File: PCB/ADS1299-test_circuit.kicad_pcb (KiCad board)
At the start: 2 copper layers, 90.4 x 96.4 mm, 111 parts, among them J1 CONN_01X07, J2 CONN_01X01_MALE, J3 CONN_01X01_MALE, P1 +5V, P10 CONN_01X03, P11 CONN_01X03, P12 CONN_01X03, P13 CONN_01X03, P14 BiasOut_C, P15 BiasOut_R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

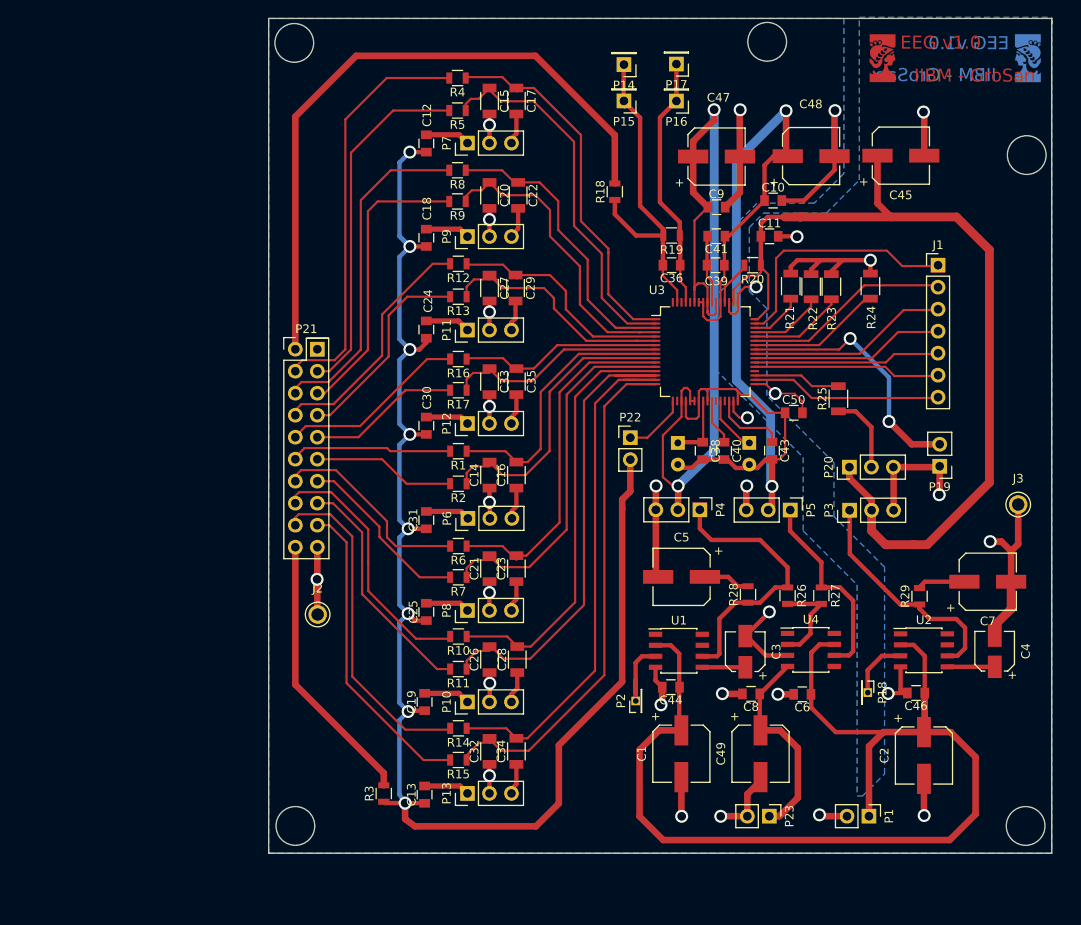
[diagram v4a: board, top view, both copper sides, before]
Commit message: Update Arduino and matlab code
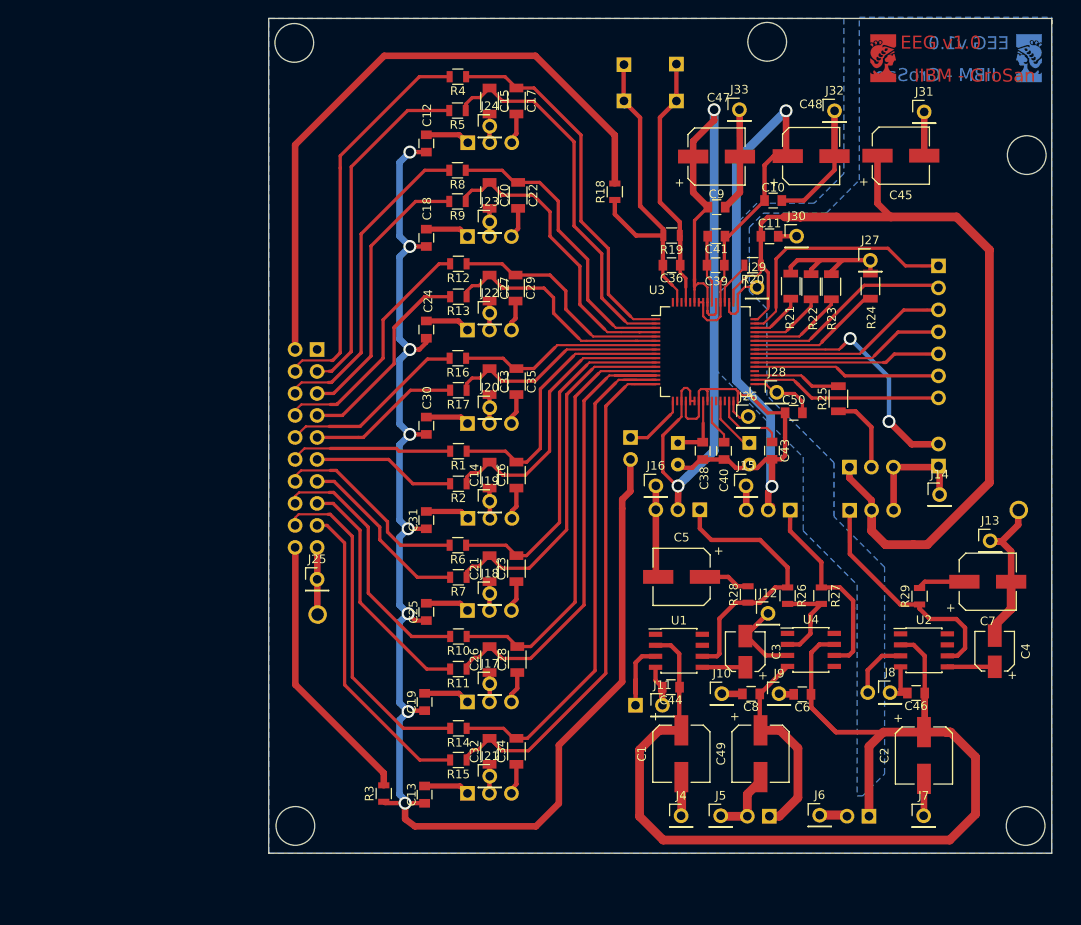
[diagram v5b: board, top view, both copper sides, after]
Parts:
- removed the G*** at (186.2, 29.0)
- removed the G*** at (202.9, 29.0)
- added G***: LOGO, LogoModules:logoFiuba_small_mirrored, F.Cu at (186.3, 29.0)
- added G***: LOGO, LogoModules:logoFiuba_small_mirrored, B.Cu at (203.1, 29.0)
- added J10: Via, Pin_Headers:Pin_Header_Straight_1x01_Pitch2.54mm, F.Cu at (167.6, 102.4)
- added J11: Via, Pin_Headers:Pin_Header_Straight_1x01_Pitch2.54mm, F.Cu at (160.8, 103.7)
- added J12: Via, Pin_Headers:Pin_Header_Straight_1x01_Pitch2.54mm, F.Cu at (173.0, 93.1)
- added J13: Via, Pin_Headers:Pin_Header_Straight_1x01_Pitch2.54mm, F.Cu at (198.6, 84.7)
- added J14: Via, Pin_Headers:Pin_Header_Straight_1x01_Pitch2.54mm, F.Cu at (192.8, 79.4)
- added J15: Via, Pin_Headers:Pin_Header_Straight_1x01_Pitch2.54mm, F.Cu at (170.4, 78.4)
- added J16: Via, Pin_Headers:Pin_Header_Straight_1x01_Pitch2.54mm, F.Cu at (160.0, 78.4)
- added J17: Via, Pin_Headers:Pin_Header_Straight_1x01_Pitch2.54mm, F.Cu at (140.8, 101.2)
- added J18: Via, Pin_Headers:Pin_Header_Straight_1x01_Pitch2.54mm, F.Cu at (140.8, 90.8)
- added J19: Via, Pin_Headers:Pin_Header_Straight_1x01_Pitch2.54mm, F.Cu at (140.8, 80.1)
- added J20: Via, Pin_Headers:Pin_Header_Straight_1x01_Pitch2.54mm, F.Cu at (140.8, 69.3)
- added J21: Via, Pin_Headers:Pin_Header_Straight_1x01_Pitch2.54mm, F.Cu at (140.8, 111.9)
- added J22: Via, Pin_Headers:Pin_Header_Straight_1x01_Pitch2.54mm, F.Cu at (140.8, 58.4)
- added J23: Via, Pin_Headers:Pin_Header_Straight_1x01_Pitch2.54mm, F.Cu at (140.8, 47.9)
- added J24: Via, Pin_Headers:Pin_Header_Straight_1x01_Pitch2.54mm, F.Cu at (140.8, 36.8)
- added J25: Via, Pin_Headers:Pin_Header_Straight_1x01_Pitch2.54mm, F.Cu at (120.9, 89.2)
- added J26: Via, Pin_Headers:Pin_Header_Straight_1x01_Pitch2.54mm, F.Cu at (170.7, 70.4)
- added J27: Via, Pin_Headers:Pin_Header_Straight_1x01_Pitch2.54mm, F.Cu at (184.8, 52.3)
- added J28: Via, Pin_Headers:Pin_Header_Straight_1x01_Pitch2.54mm, F.Cu at (174.0, 67.6)
- added J29: Via, Pin_Headers:Pin_Header_Straight_1x01_Pitch2.54mm, F.Cu at (171.7, 55.4)
- added J30: Via, Pin_Headers:Pin_Header_Straight_1x01_Pitch2.54mm, F.Cu at (176.3, 49.5)
- added J31: Via, Pin_Headers:Pin_Header_Straight_1x01_Pitch2.54mm, F.Cu at (191.0, 35.2)
- added J32: Via, Pin_Headers:Pin_Header_Straight_1x01_Pitch2.54mm, F.Cu at (180.7, 35.1)
- added J33: Via, Pin_Headers:Pin_Header_Straight_1x01_Pitch2.54mm, F.Cu at (169.7, 34.9)
- added J4: Via, Pin_Headers:Pin_Header_Straight_1x01_Pitch2.54mm, F.Cu at (162.9, 116.5)
- added J5: Via, Pin_Headers:Pin_Header_Straight_1x01_Pitch2.54mm, F.Cu at (167.5, 116.5)
- added J6: Via, Pin_Headers:Pin_Header_Straight_1x01_Pitch2.54mm, F.Cu at (178.9, 116.4)
- added J7: Via, Pin_Headers:Pin_Header_Straight_1x01_Pitch2.54mm, F.Cu at (190.9, 116.5)
- added J8: Via, Pin_Headers:Pin_Header_Straight_1x01_Pitch2.54mm, F.Cu at (187.1, 102.2)
- added J9: Via, Pin_Headers:Pin_Header_Straight_1x01_Pitch2.54mm, F.Cu at (174.2, 102.4)
- J1: value CONN_01X07 -> OUT; moved to B.Cu
- J2, J3: value CONN_01X01_MALE -> GND; moved to B.Cu
- P1, P14, P15, P16, P17, P19, P20, P22, P23, P3, P4, P5: moved to B.Cu
- P10: value CONN_01X03 -> IN2; moved to B.Cu
- P11: value CONN_01X03 -> IN6; moved to B.Cu
- P12: value CONN_01X03 -> IN5; moved to B.Cu
- P13: value CONN_01X03 -> IN1; moved to B.Cu
- P18, P2: footprint Pin_Headers:Pin_Header_Straight_1x01_Pitch1.27mm -> Pin_Headers:Pin_Header_Straight_1x01_Pitch2.54mm; moved to B.Cu
- P21: footprint Pin_Headers_Mirrored:Pin_Header_Straight_2x10_Pitch2.54mm_Mirrored -> Pin_Headers:Pin_Header_Straight_2x10_Pitch2.54mm; moved to B.Cu
- P6: value CONN_01X03 -> IN4; moved to B.Cu
- P7: value CONN_01X03 -> IN8; moved to B.Cu
- P8: value CONN_01X03 -> IN3; moved to B.Cu
- P9: value CONN_01X03 -> IN7; moved to B.Cu
- moved P21 2.51 mm to (120.9, 62.6), turned to 180 degrees
- moved J3 0.64 mm to (201.9, 81.2)
- moved P2 0.50 mm to (157.7, 103.7), turned to 270 degrees
- moved R4 0.16 mm to (137.2, 31.1)
- moved P19 0.14 mm to (192.7, 76.1), turned to 0 degrees
- moved R6 0.12 mm to (137.2, 85.2)
- moved R16 0.11 mm to (137.2, 63.6)
- moved J1 0.09 mm to (192.7, 53.0), turned to 180 degrees
- moved P7 0.06 mm to (138.3, 38.7), turned to 270 degrees
- turned P22 to 180 degrees
- turned P1 to 90 degrees
- turned P10 to 270 degrees
- turned P11 to 270 degrees
- turned P12 to 270 degrees
- turned P13 to 270 degrees
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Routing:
- net +5: track 130.2 -> 216.9 mm
- net Net-(C12-Pad2): track 237.0 -> 310.2 mm
- net Net-(C32-Pad2): track 62.9 -> 111.5 mm
- net Net-(C34-Pad2): track 62.0 -> 105.2 mm
- net Net-(C26-Pad2): track 57.5 -> 95.0 mm
- net Net-(C28-Pad2): track 49.4 -> 86.6 mm
- net Net-(C17-Pad1): track 42.9 -> 71.9 mm
- net Net-(C15-Pad1): track 43.7 -> 69.8 mm
- net GND: track 199.2 -> 224.8 mm, vias 30 -> 0
- net Net-(C22-Pad1): track 34.2 -> 59.1 mm
- net Net-(C21-Pad2): track 43.4 -> 66.5 mm
- net Net-(C23-Pad2): track 40.6 -> 62.3 mm
- net Net-(C16-Pad2): track 32.2 -> 48.6 mm
- net Net-(C14-Pad2): track 33.7 -> 49.1 mm
- net Net-(C20-Pad1): track 35.1 -> 49.8 mm
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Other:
- net class Default: clearance 0.1 -> 0.21
- rule trace_clearance: 0.1 -> 0.21
